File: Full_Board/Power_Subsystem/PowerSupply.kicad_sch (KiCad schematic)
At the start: 10 parts, among them J1 KLDHCX-8-0202-A

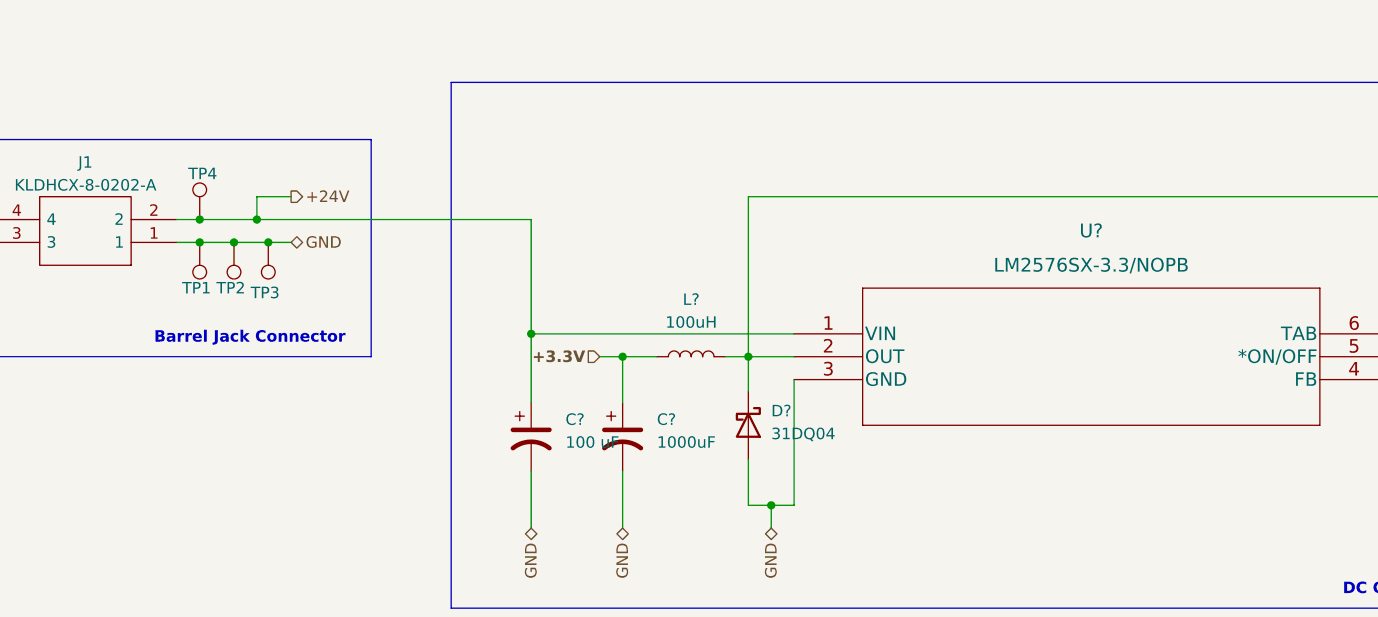
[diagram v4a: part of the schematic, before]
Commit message: Add digikey/mouser components to stepper and button subsystems
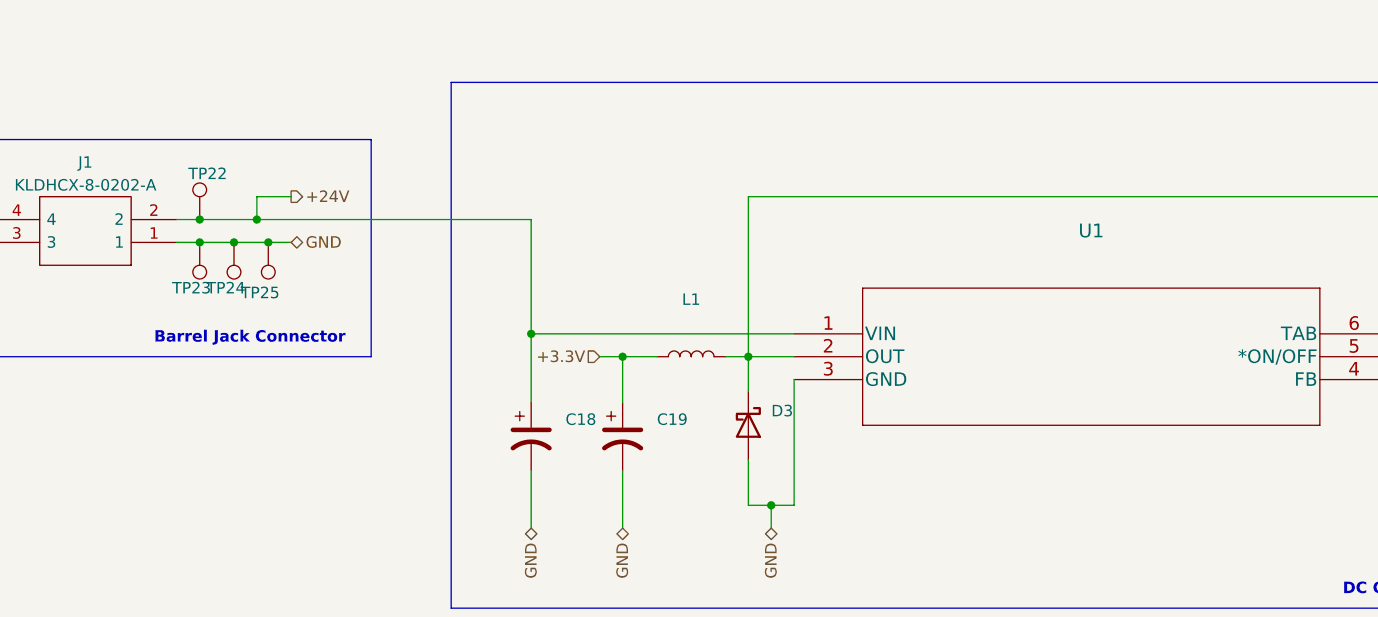
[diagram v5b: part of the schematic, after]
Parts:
- C18: renamed from C?; value 100 uF -> (none)
- C19: renamed from C?; value 1000uF -> (none)
- D3: renamed from D?; value 31DQ04 -> (none)
- L1: renamed from L?; value 100uH -> (none)
- TP23: renamed from TP1; footprint TestPoint:TestPoint_Keystone_5010-5014_Multipurpose -> (none)
- TP24: renamed from TP2; footprint TestPoint:TestPoint_Keystone_5010-5014_Multipurpose -> (none)
- TP25: renamed from TP3; footprint TestPoint:TestPoint_Keystone_5010-5014_Multipurpose -> (none)
- U1: renamed from U?; value LM2576SX-3.3/NOPB -> (none); footprint TS5B_TEX -> (none)
- renumbered TP4 to TP22
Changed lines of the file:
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@@
   )
   (hierarchical_label "+3.3V" (shape input) (at 133.35 95.25 180)
-    (effects (font (size 1.27 1.27) bold) (justify right))
+    (effects (font (size 1.27 1.27)) (justify right))
   )
   (hierarchical_label "GND" (shape bidirectional) (at 135.89 114.3 270)
@@
   (symbol (lib_id "Connector:TestPoint") (at 88.9 82.55 180) (unit 1)
     (in_bom yes) (on_board yes)
-    (property "Reference" "TP1" (id 0) (at 90.17 87.63 0)
+    (property "Reference" "TP23" (id 0) (at 90.17 87.63 0)
       (effects (font (size 1.27 1.27)) (justify left))
     )
@@
       (effects (font (size 1.27 1.27)) (justify left) hide)
     )
-    (property "Footprint" "TestPoint:TestPoint_Keystone_5010-5014_Multipurpose" (id 2) (at 83.82 82.55 0)
+    (property "Footprint" "" (id 2) (at 83.82 82.55 0)
       (effects (font (size 1.27 1.27)) hide)
     )
@@
   (symbol (lib_id "Connector:TestPoint") (at 88.9 80.01 0) (unit 1)
     (in_bom yes) (on_board yes)
-    (property "Reference" "TP4" (id 0) (at 87.63 74.93 0)
+    (property "Reference" "TP22" (id 0) (at 87.63 74.93 0)
       (effects (font (size 1.27 1.27)) (justify left))
     )
@@
   (symbol (lib_id "Connector:TestPoint") (at 92.71 82.55 180) (unit 1)
     (in_bom yes) (on_board yes)
-    (property "Reference" "TP2" (id 0) (at 93.98 87.63 0)
+    (property "Reference" "TP24" (id 0) (at 93.98 87.63 0)
       (effects (font (size 1.27 1.27)) (justify left))
     )
@@
       (effects (font (size 1.27 1.27)) (justify left) hide)
     )
-    (property "Footprint" "TestPoint:TestPoint_Keystone_5010-5014_Multipurpose" (id 2) (at 87.63 82.55 0)
+    (property "Footprint" "" (id 2) (at 87.63 82.55 0)
       (effects (font (size 1.27 1.27)) hide)
     )
@@
   (symbol (lib_id "Device:L") (at 143.51 95.25 90) (unit 1)
     (in_bom yes) (on_board yes) (fields_autoplaced)
-    (property "Reference" "L?" (id 0) (at 143.51 88.9 90))
-    (property "Value" "100uH" (id 1) (at 143.51 91.44 90))
+    (property "Reference" "L1" (id 0) (at 143.51 88.9 90))
+    (property "Value" "" (id 1) (at 143.51 91.44 90))
     (property "Footprint" "" (id 2) (at 143.51 95.25 0)
       (effects (font (size 1.27 1.27)) hide)
@@
   (symbol (lib_id "Device:C_Polarized_US") (at 125.73 104.14 0) (unit 1)
     (in_bom yes) (on_board yes) (fields_autoplaced)
-    (property "Reference" "C?" (id 0) (at 129.54 102.2349 0)
-      (effects (font (size 1.27 1.27)) (justify left))
-    )
-    (property "Value" "100 uF" (id 1) (at 129.54 104.7749 0)
+    (property "Reference" "C18" (id 0) (at 129.54 102.2349 0)
+      (effects (font (size 1.27 1.27)) (justify left))
+    )
+    (property "Value" "" (id 1) (at 129.54 104.7749 0)
       (effects (font (size 1.27 1.27)) (justify left))
     )
@@
   (symbol (lib_id "LM25776SX-3-3-NOPB:LM2576SX-3.3{slash}NOPB") (at 154.94 92.71 0) (unit 1)
     (in_bom yes) (on_board yes) (fields_autoplaced)
-    (property "Reference" "U?" (id 0) (at 187.96 81.28 0)
+    (property "Reference" "U1" (id 0) (at 187.96 81.28 0)
       (effects (font (size 1.524 1.524)))
     )
-    (property "Value" "LM2576SX-3.3/NOPB" (id 1) (at 187.96 85.09 0)
+    (property "Value" "" (id 1) (at 187.96 85.09 0)
       (effects (font (size 1.524 1.524)))
     )
-    (property "Footprint" "TS5B_TEX" (id 2) (at 187.96 86.614 0)
+    (property "Footprint" "" (id 2) (at 187.96 86.614 0)
       (effects (font (size 1.524 1.524)) hide)
     )
@@
   (symbol (lib_id "Device:C_Polarized_US") (at 135.89 104.14 0) (unit 1)
     (in_bom yes) (on_board yes) (fields_autoplaced)
-    (property "Reference" "C?" (id 0) (at 139.7 102.2349 0)
-      (effects (font (size 1.27 1.27)) (justify left))
-    )
-    (property "Value" "1000uF" (id 1) (at 139.7 104.7749 0)
+    (property "Reference" "C19" (id 0) (at 139.7 102.2349 0)
+      (effects (font (size 1.27 1.27)) (justify left))
+    )
+    (property "Value" "" (id 1) (at 139.7 104.7749 0)
       (effects (font (size 1.27 1.27)) (justify left))
     )
@@
   (symbol (lib_id "Connector:TestPoint") (at 96.52 82.55 180) (unit 1)
     (in_bom yes) (on_board yes)
-    (property "Reference" "TP3" (id 0) (at 97.79 88.9 0)
+    (property "Reference" "TP25" (id 0) (at 97.79 88.9 0)
       (effects (font (size 1.27 1.27)) (justify left top))
     )
@@
       (effects (font (size 1.27 1.27)) (justify left) hide)
     )
-    (property "Footprint" "TestPoint:TestPoint_Keystone_5010-5014_Multipurpose" (id 2) (at 91.44 82.55 0)
+    (property "Footprint" "" (id 2) (at 91.44 82.55 0)
       (effects (font (size 1.27 1.27)) hide)
     )
@@
   (symbol (lib_id "Device:D_Schottky") (at 149.86 102.87 270) (unit 1)
     (in_bom yes) (on_board yes) (fields_autoplaced)
-    (property "Reference" "D?" (id 0) (at 152.4 101.2824 90)
-      (effects (font (size 1.27 1.27)) (justify left))
-    )
-    (property "Value" "31DQ04" (id 1) (at 152.4 103.8224 90)
-      (effects (font (size 1.27 1.27)) (justify left))
-    )
+    (property "Reference" "D3" (id 0) (at 152.4 101.2824 90)
+      (effects (font (size 1.27 1.27)) (justify left))
+    )
+    (property "Value" "" (id 1) (at 152.4 103.8224 90)
+      (effects (font (size 1.27 1.27)) (justify left))
+    )

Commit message: Add files via upload
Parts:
- C18: value (none) -> 100 uF; footprint (none) -> Capacitor_SMD:CP_Elec_3x5.3
- C19: value (none) -> 1000uF; footprint (none) -> Capacitor_SMD:CP_Elec_3x5.3
- D3: value (none) -> 31DQ04; footprint (none) -> Diode_SMD:D_0201_0603Metric
- J1: footprint KLDHCX80202A -> Power_Connector_KLDHCX:KLDHCX80202A
- L1: value (none) -> 100uH
- TP23, TP24, TP25: footprint (none) -> TestPoint:TestPoint_Keystone_5010-5014_Multipurpose
- U1: value (none) -> LM2576SX-3.3/NOPB
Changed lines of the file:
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@@
   (junction (at 88.9 80.01) (diameter 0) (color 0 0 0 0)
+  )
+  (junction (at 154.94 109.22) (diameter 0) (color 0 0 0 0)
+  )
+  (junction (at 133.35 92.71) (diameter 0) (color 0 0 0 0)
+  )
+  (junction (at 152.4 95.25) (diameter 0) (color 0 0 0 0)
   )
   (junction (at 152.4 111.76) (diameter 0) (color 0 0 0 0)
@@
     (stroke (width 0) (type default) (color 0 0 0 0))
   )
+  (wire (pts (xy 152.4 95.25) (xy 154.94 95.25))
+    (stroke (width 0) (type default) (color 0 0 0 0))
+  )
   (wire (pts (xy 135.89 95.25) (xy 135.89 100.33))
     (stroke (width 0) (type default) (color 0 0 0 0))
@@
     (stroke (width 0) (type default) (color 0 0 0 0))
   )
-  (wire (pts (xy 154.94 97.79) (xy 154.94 111.76))
+  (wire (pts (xy 154.94 109.22) (xy 154.94 111.76))
+    (stroke (width 0) (type default) (color 0 0 0 0))
+  )
+  (wire (pts (xy 154.94 97.79) (xy 154.94 109.22))
     (stroke (width 0) (type default) (color 0 0 0 0))
   )
@@
     (stroke (width 0) (type default) (color 0 0 0 0))
   )
+  (wire (pts (xy 152.4 90.17) (xy 152.4 95.25))
+    (stroke (width 0) (type default) (color 0 0 0 0))
+  )
   (wire (pts (xy 125.73 92.71) (xy 125.73 80.01))
     (stroke (width 0) (type default) (color 0 0 0 0))
@@
     (stroke (width 0) (type default) (color 0 0 0 0))
   )
-  (wire (pts (xy 154.94 92.71) (xy 125.73 92.71))
+  (wire (pts (xy 154.94 92.71) (xy 133.35 92.71))
     (stroke (width 0) (type default) (color 0 0 0 0))
   )
@@
     (stroke (width 0) (type default) (color 0 0 0 0))
   )
-  (wire (pts (xy 149.86 95.25) (xy 154.94 95.25))
+  (wire (pts (xy 149.86 95.25) (xy 152.4 95.25))
+    (stroke (width 0) (type default) (color 0 0 0 0))
+  )
+  (wire (pts (xy 125.73 92.71) (xy 133.35 92.71))
     (stroke (width 0) (type default) (color 0 0 0 0))
   )
@@
     (effects (font (size 1.27 1.27)) (justify right))
   )
+  (symbol (lib_id "power:PWR_FLAG") (at 154.94 109.22 270) (unit 1)
+    (in_bom yes) (on_board yes) (fields_autoplaced)
+    (property "Reference" "#FLG02" (id 0) (at 156.845 109.22 0)
+      (effects (font (size 1.27 1.27)) hide)
+    )
+    (property "Value" "PWR_FLAG" (id 1) (at 158.75 109.2199 90)
+      (effects (font (size 1.27 1.27)) (justify left))
+    )
+    (property "Footprint" "" (id 2) (at 154.94 109.22 0)
+      (effects (font (size 1.27 1.27)) hide)
+    )
+    (property "Datasheet" "~" (id 3) (at 154.94 109.22 0)
+      (effects (font (size 1.27 1.27)) hide)
+    )
+    (pin "1")
+  )
   (symbol (lib_id "KLDHCX-8-0202-A:KLDHCX-8-0202-A") (at 86.36 82.55 180) (unit 1)
     (in_bom yes) (on_board yes)
     (property "Reference" "J1" (id 0) (at 76.2 73.66 0))
     (property "Value" "KLDHCX-8-0202-A" (id 1) (at 76.2 76.2 0))
-    (property "Footprint" "KLDHCX80202A" (id 2) (at 69.85 85.09 0)
+    (property "Footprint" "Power_Connector_KLDHCX:KLDHCX80202A" (id 2) (at 69.85 85.09 0)
       (effects (font (size 1.27 1.27)) (justify left) hide)
     )
@@
       (effects (font (size 1.27 1.27)) (justify left) hide)
     )
-    (property "Footprint" "" (id 2) (at 83.82 82.55 0)
+    (property "Footprint" "TestPoint:TestPoint_Keystone_5010-5014_Multipurpose" (id 2) (at 83.82 82.55 0)
       (effects (font (size 1.27 1.27)) hide)
     )
@@
       (effects (font (size 1.27 1.27)) (justify left) hide)
     )
-    (property "Footprint" "" (id 2) (at 87.63 82.55 0)
+    (property "Footprint" "TestPoint:TestPoint_Keystone_5010-5014_Multipurpose" (id 2) (at 87.63 82.55 0)
       (effects (font (size 1.27 1.27)) hide)
     )
@@
     (in_bom yes) (on_board yes) (fields_autoplaced)
     (property "Reference" "L1" (id 0) (at 143.51 88.9 90))
-    (property "Value" "" (id 1) (at 143.51 91.44 90))
+    (property "Value" "100uH" (id 1) (at 143.51 91.44 90))
     (property "Footprint" "" (id 2) (at 143.51 95.25 0)
       (effects (font (size 1.27 1.27)) hide)
@@
       (effects (font (size 1.27 1.27)) (justify left))
     )
-    (property "Value" "" (id 1) (at 129.54 104.7749 0)
-      (effects (font (size 1.27 1.27)) (justify left))
-    )
-    (property "Footprint" "" (id 2) (at 125.73 104.14 0)
+    (property "Value" "100 uF" (id 1) (at 129.54 104.7749 0)
+      (effects (font (size 1.27 1.27)) (justify left))
+    )
+    (property "Footprint" "Capacitor_SMD:CP_Elec_3x5.3" (id 2) (at 125.73 104.14 0)
       (effects (font (size 1.27 1.27)) hide)
     )
@@
       (effects (font (size 1.524 1.524)))
     )
-    (property "Value" "" (id 1) (at 187.96 85.09 0)
+    (property "Value" "LM2576SX-3.3/NOPB" (id 1) (at 187.96 85.09 0)
       (effects (font (size 1.524 1.524)))
     )
@@
       (effects (font (size 1.27 1.27)) (justify left))
     )
-    (property "Value" "" (id 1) (at 139.7 104.7749 0)
-      (effects (font (size 1.27 1.27)) (justify left))
-    )
-    (property "Footprint" "" (id 2) (at 135.89 104.14 0)
+    (property "Value" "1000uF" (id 1) (at 139.7 104.7749 0)
+      (effects (font (size 1.27 1.27)) (justify left))
+    )
+    (property "Footprint" "Capacitor_SMD:CP_Elec_3x5.3" (id 2) (at 135.89 104.14 0)
       (effects (font (size 1.27 1.27)) hide)
     )
@@
     (pin "1")
     (pin "2")
+  )
+  (symbol (lib_id "power:PWR_FLAG") (at 133.35 92.71 0) (unit 1)
+    (in_bom yes) (on_board yes)
+    (property "Reference" "#FLG01" (id 0) (at 133.35 90.805 0)
+      (effects (font (size 1.27 1.27)) hide)
+    )
+    (property "Value" "PWR_FLAG" (id 1) (at 129.54 88.9 0)
+      (effects (font (size 1.27 1.27)) (justify left))
+    )
+    (property "Footprint" "" (id 2) (at 133.35 92.71 0)
+      (effects (font (size 1.27 1.27)) hide)
+    )
+    (property "Datasheet" "~" (id 3) (at 133.35 92.71 0)
+      (effects (font (size 1.27 1.27)) hide)
+    )
+    (pin "1")
+  )
+  (symbol (lib_id "power:PWR_FLAG") (at 152.4 90.17 0) (unit 1)
+    (in_bom yes) (on_board yes)
+    (property "Reference" "#FLG0101" (id 0) (at 152.4 88.265 0)
+      (effects (font (size 1.27 1.27)) hide)
+    )
+    (property "Value" "PWR_FLAG" (id 1) (at 152.4 86.36 0)
+      (effects (font (size 1.27 1.27)) (justify left))
+    )
+    (property "Footprint" "" (id 2) (at 152.4 90.17 0)
+      (effects (font (size 1.27 1.27)) hide)
+    )
+    (property "Datasheet" "~" (id 3) (at 152.4 90.17 0)
+      (effects (font (size 1.27 1.27)) hide)
+    )
+    (pin "1")
   )
   (symbol (lib_id "Connector:TestPoint") (at 96.52 82.55 180) (unit 1)
@@
       (effects (font (size 1.27 1.27)) (justify left) hide)
     )
-    (property "Footprint" "" (id 2) (at 91.44 82.55 0)
+    (property "Footprint" "TestPoint:TestPoint_Keystone_5010-5014_Multipurpose" (id 2) (at 91.44 82.55 0)
       (effects (font (size 1.27 1.27)) hide)
     )
@@
       (effects (font (size 1.27 1.27)) (justify left))
     )
-    (property "Value" "" (id 1) (at 152.4 103.8224 90)
-      (effects (font (size 1.27 1.27)) (justify left))
-    )
-    (property "Footprint" "" (id 2) (at 149.86 102.87 0)
-      (effects (font (size 1.27 1.27)) hide)
-    )
+    (property "Value" "31DQ04" (id 1) (at 152.4 103.8224 90)
+      (effects (font (size 1.27 1.27)) (justify left))
+    )
+    (property "Footprint" "Diode_SMD:D_0201_0603Metric" (id 2) (at 149.86 102.87 0)
+      (effects (font (size 1.27 1.27)) hide)
+    )

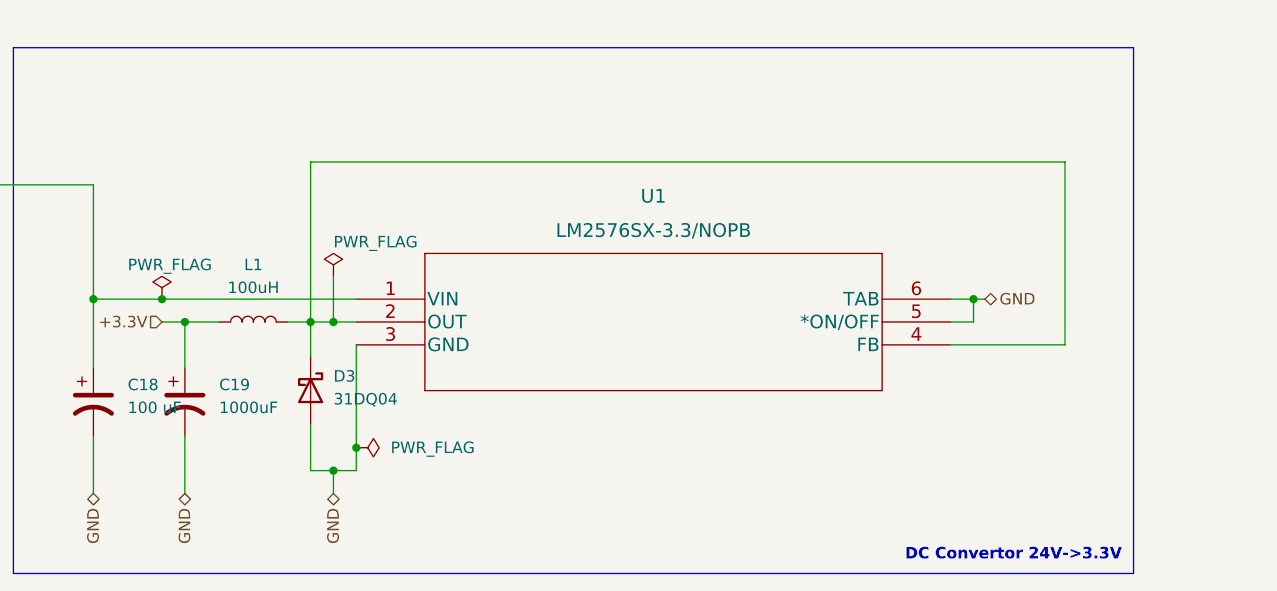
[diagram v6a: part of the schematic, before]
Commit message: Added specific components for the power subsheet
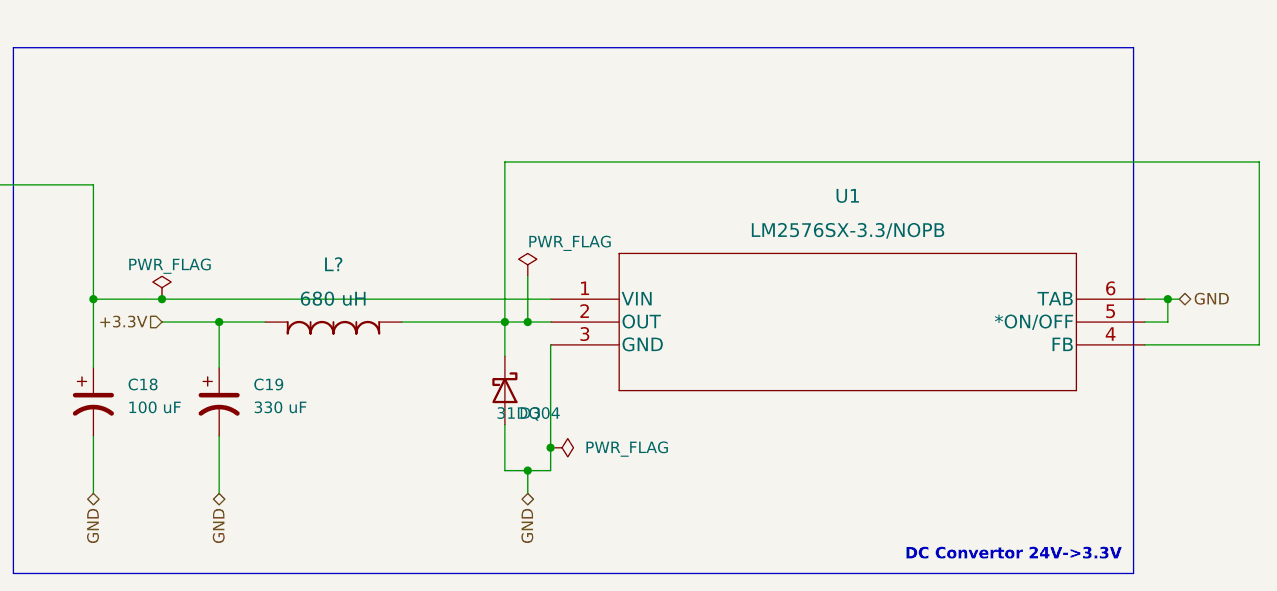
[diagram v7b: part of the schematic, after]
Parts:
- removed L1: 100uH, symbol Device:L
- added L?: 680 uH, IND_BOURNS_SRR1210, symbol SRR1210-681M:SRR1210-681M
- C18: Digikey Link (none) -> https://www.digikey.com/en/products/detail/w%C3%BCrth-elekt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; Digikey Part Number (none) -> 732-8942-1-ND; Manufacturers Part Number (none) -> 860020573008
- C19: value 1000uF -> 330 uF; footprint Capacitor_SMD:CP_Elec_3x5.3 -> Capacitor_THT:CP_Radial_D10.0mm_P5.00mm; Digikey Link (none) -> https://www.digikey.com/en/products/detail/cornell-dubilier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; Digikey Part Number (none) -> 338-1748-ND; Manufacturers Part Number (none) -> SEK331M050ST
- D3: footprint Diode_SMD:D_0201_0603Metric -> Diode_THT:D_DO-201AD_P15.24mm_Horizontal; Digikey Link (none) -> https://www.digikey.com/en/products/detail/smc-diode-soluti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; Digikey Part Number (none) -> 1655-31DQ04CT-ND; Manufacturers Part Number (none) -> 31DQ04
- U1: footprint (none) -> LM2576SX-3-3-NOPB:LM2576SX-3.3&slash_NOPB
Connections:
- net +3.3V: now also L?.1
- net at D3.1 (K), U1.2 (OUT), U1.4 (FB): now also L?.2
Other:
- moved on the sheet: C19, D3, U1
